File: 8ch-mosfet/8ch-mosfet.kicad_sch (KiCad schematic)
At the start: 7 parts, among them U1 ESP32-DEVKITC

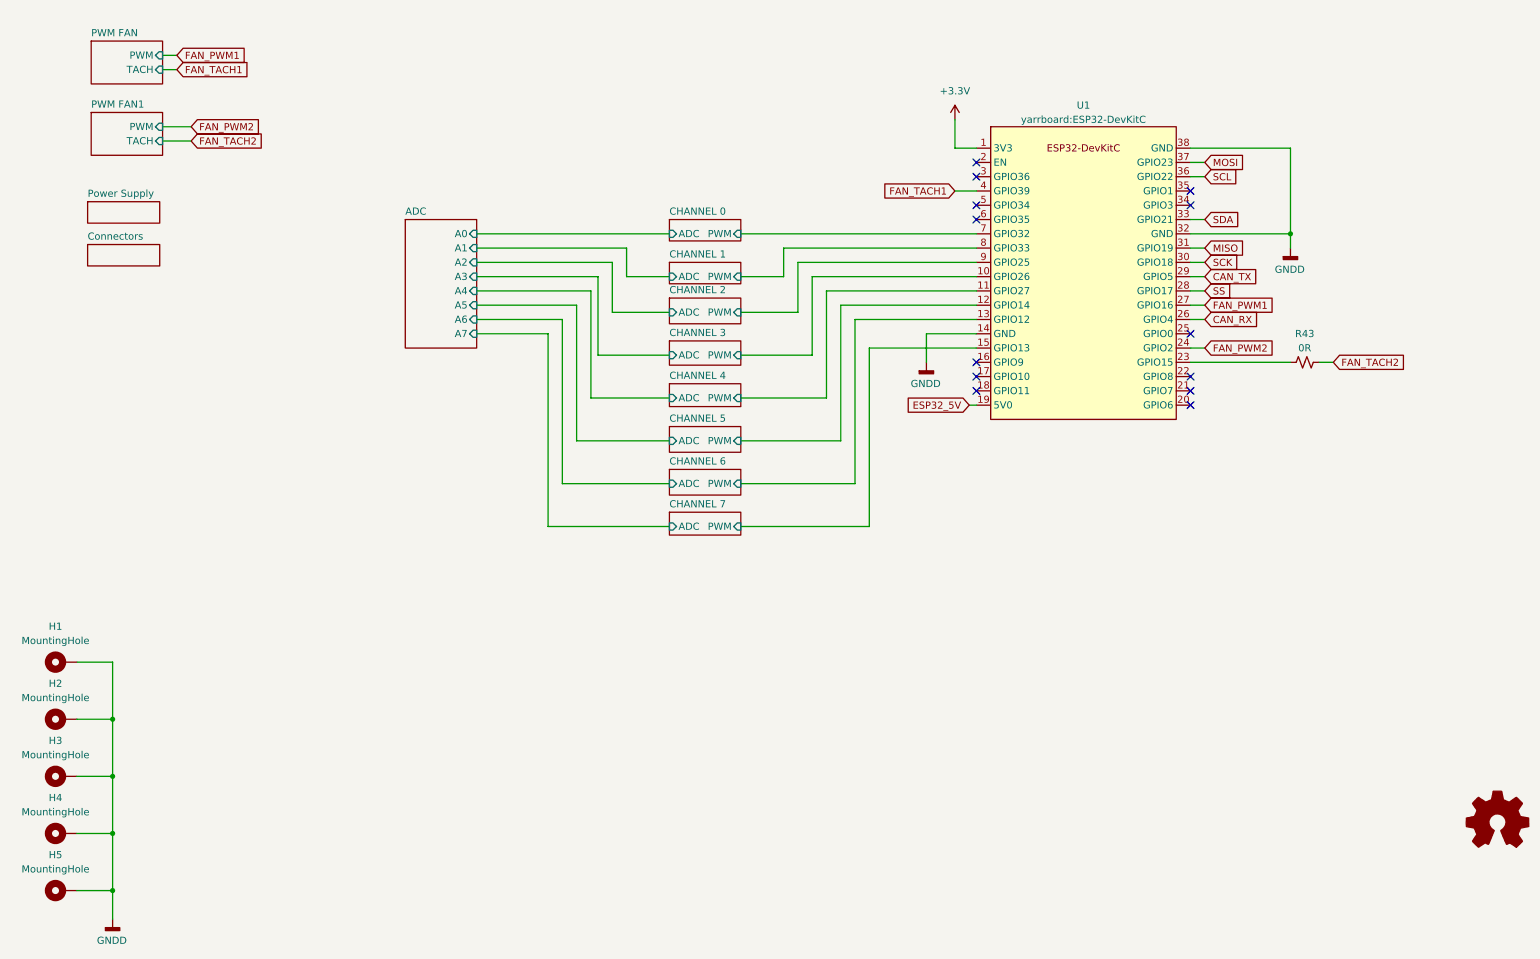
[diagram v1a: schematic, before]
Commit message: changed to new s3 module
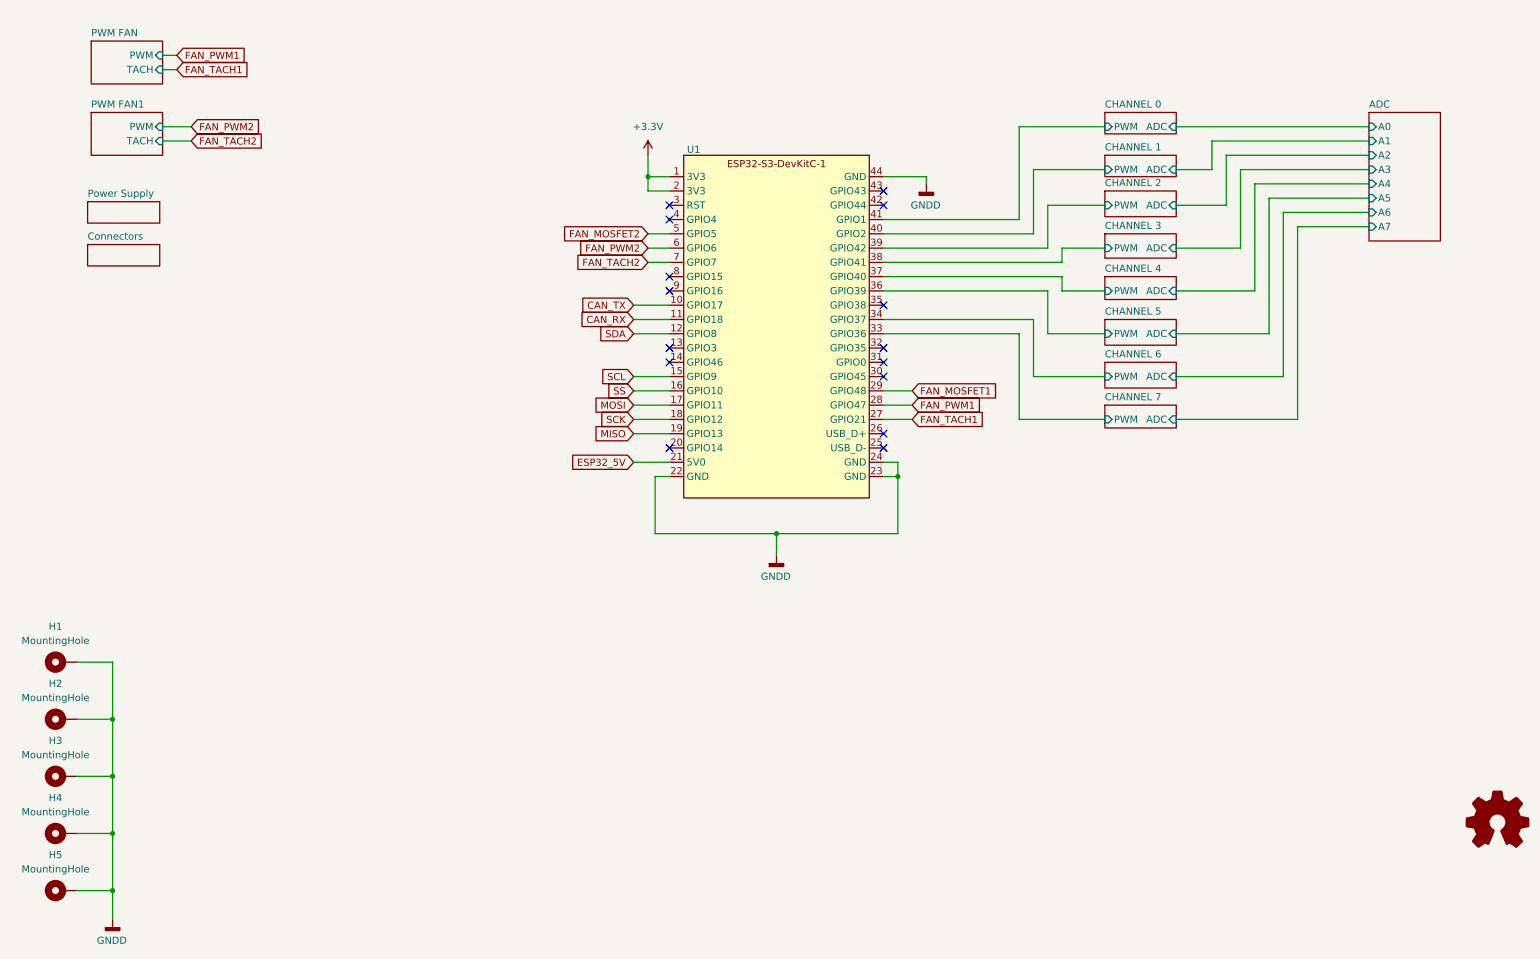
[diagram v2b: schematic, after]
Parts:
- removed R43: 0R, Resistor_SMD:R_0805_2012Metric_Pad1.20x1.40mm_HandSolder, symbol Device:R_Small_US
- removed U1: ESP32-DEVKITC, yarrboard:ESP32-DevKitC, symbol gnarboard:ESP32_DevKit_C
- added U1: ~, yarrboard:Waveshare-ESP32-S3-dev-kit, symbol yarrboard:ESP32-S3-DevKitC-1
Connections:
- net +3.3V: now also U1.1 (3V3), U1.2 (3V3)
- net CAN_RX: now also U1.11 (GPIO18)
- net CAN_TX: now also U1.10 (GPIO17)
- net CHANNEL 0/PWM: now also U1.41 (GPIO1)
- net CHANNEL 1/PWM: now also U1.40 (GPIO2)
- net CHANNEL 2/PWM: now also U1.39 (GPIO42)
- net CHANNEL 3/PWM: now also U1.38 (GPIO41)
- net CHANNEL 4/PWM: now also U1.37 (GPIO40)
- net CHANNEL 5/PWM: now also U1.36 (GPIO39)
- net CHANNEL 6/PWM: now also U1.34 (GPIO37)
- net CHANNEL 7/PWM: now also U1.33 (GPIO36)
- net ESP32_5V: now also U1.21 (5V0)
- net FAN_PWM1: now also U1.28 (GPIO47)
- net FAN_PWM2: now also U1.6 (GPIO6)
- net FAN_TACH1: now also U1.27 (GPIO21)
- net FAN_TACH2: now also U1.7 (GPIO7)
- net GNDD: now also U1.22 (GND), U1.23 (GND), U1.24 (GND), U1.44 (GND)
- net MISO: now also U1.19 (GPIO13)
- net MOSI: now also U1.17 (GPIO11)
- net SCK: now also U1.18 (GPIO12)
- net SCL: now also U1.15 (GPIO9)
- net SDA: now also U1.12 (GPIO8)
- net SS: now also U1.16 (GPIO10)
- new net FAN_MOSFET1: U1.29 (GPIO48)
- new net FAN_MOSFET2: U1.5 (GPIO5)
- no-connect marks 13 -> 15

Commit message: more progress on new 8ch board.
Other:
- sheet PWM FAN ports: added MOSFET; removed none
- sheet PWM FAN1 ports: added MOSFET; removed none
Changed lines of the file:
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@@
 	(wire
 		(pts
-			(xy 40.64 40.64) (xy 43.18 40.64)
+			(xy 40.64 38.1) (xy 45.72 38.1)
 		)
 		(stroke
@@
 	(wire
 		(pts
+			(xy 40.64 55.88) (xy 45.72 55.88)
+		)
+		(stroke
+			(width 0)
+			(type default)
+		)
+	)
+	(wire
+		(pts
 			(xy 130.81 62.23) (xy 127 62.23)
 		)
@@
 	(wire
 		(pts
+			(xy 40.64 40.64) (xy 45.72 40.64)
+		)
+		(stroke
+			(width 0)
+			(type default)
+		)
+	)
+	(wire
+		(pts
 			(xy 171.45 110.49) (xy 171.45 113.03)
 		)
@@
 	(wire
 		(pts
-			(xy 40.64 38.1) (xy 43.18 38.1)
+			(xy 40.64 35.56) (xy 45.72 35.56)
 		)
 		(stroke
@@
 		)
 	)
+	(global_label "FAN_MOSFET1"
+		(shape input)
+		(at 45.72 40.64 0)
+		(fields_autoplaced yes)
+		(effects
+			(font
+				(size 1.27 1.27)
+			)
+			(justify left)
+		)
+		(property "Intersheetrefs" "${INTERSHEET_REFS}"
+			(at 61.5866 40.64 0)
+			(effects
+				(font
+					(size 1.27 1.27)
+				)
+				(justify left)
+				(hide yes)
+			)
+		)
+	)
 	(global_label "FAN_PWM1"
 		(shape input)
@@
 	(global_label "FAN_PWM1"
 		(shape input)
-		(at 43.18 38.1 0)
+		(at 45.72 35.56 0)
 		(fields_autoplaced yes)
 		(effects
@@
 		)
 		(property "Intersheetrefs" "${INTERSHEET_REFS}"
-			(at 56.0228 38.1 0)
+			(at 58.5628 35.56 0)
 			(effects
 				(font
@@
 		)
 	)
+	(global_label "FAN_MOSFET2"
+		(shape input)
+		(at 45.72 55.88 0)
+		(fields_autoplaced yes)
+		(effects
+			(font
+				(size 1.27 1.27)
+			)
+			(justify left)
+		)
+		(property "Intersheetrefs" "${INTERSHEET_REFS}"
+			(at 61.5866 55.88 0)
+			(effects
+				(font
+					(size 1.27 1.27)
+				)
+				(justify left)
+				(hide yes)
+			)
+		)
+	)
 	(global_label "FAN_PWM2"
 		(shape input)
@@
 	(global_label "FAN_TACH1"
 		(shape input)
-		(at 43.18 40.64 0)
+		(at 45.72 38.1 0)
 		(fields_autoplaced yes)
 		(effects
@@
 		)
 		(property "Intersheetrefs" "${INTERSHEET_REFS}"
-			(at 56.5067 40.64 0)
+			(at 59.0467 38.1 0)
 			(effects
 				(font
@@
 	(sheet
 		(at 27.94 48.26)
-		(size 12.7 7.62)
+		(size 12.7 10.16)
 		(fields_autoplaced yes)
 		(stroke
@@
 		)
 		(property "Sheetfile" "pwm fan.kicad_sch"
-			(at 27.94 56.4646 0)
+			(at 27.94 59.0046 0)
 			(effects
 				(font
@@
 		(pin "TACH" input
 			(at 40.64 53.34 0)
+			(effects
+				(font
+					(size 1.27 1.27)
+				)
+				(justify right)
+			)
+		)
+		(pin "MOSFET" input
+			(at 40.64 55.88 0)
 			(effects
 				(font
@@
 	)
 	(sheet
-		(at 27.94 35.56)
-		(size 12.7 7.62)
+		(at 27.94 33.02)
+		(size 12.7 9.906)
 		(fields_autoplaced yes)
 		(stroke
@@
 		)
 		(property "Sheetname" "PWM FAN"
-			(at 27.94 34.8484 0)
+			(at 27.94 32.3084 0)
 			(effects
 				(font
@@
 		)
 		(property "Sheetfile" "pwm fan.kicad_sch"
-			(at 27.94 43.7646 0)
+			(at 27.94 43.5106 0)
 			(effects
 				(font
@@
 		)
 		(pin "PWM" input
+			(at 40.64 35.56 0)
+			(effects
+				(font
+					(size 1.27 1.27)
+				)
+				(justify right)
+			)
+		)
+		(pin "TACH" input
 			(at 40.64 38.1 0)
 			(effects
@@
 			)
 		)
-		(pin "TACH" input
+		(pin "MOSFET" input
 			(at 40.64 40.64 0)
 			(effects

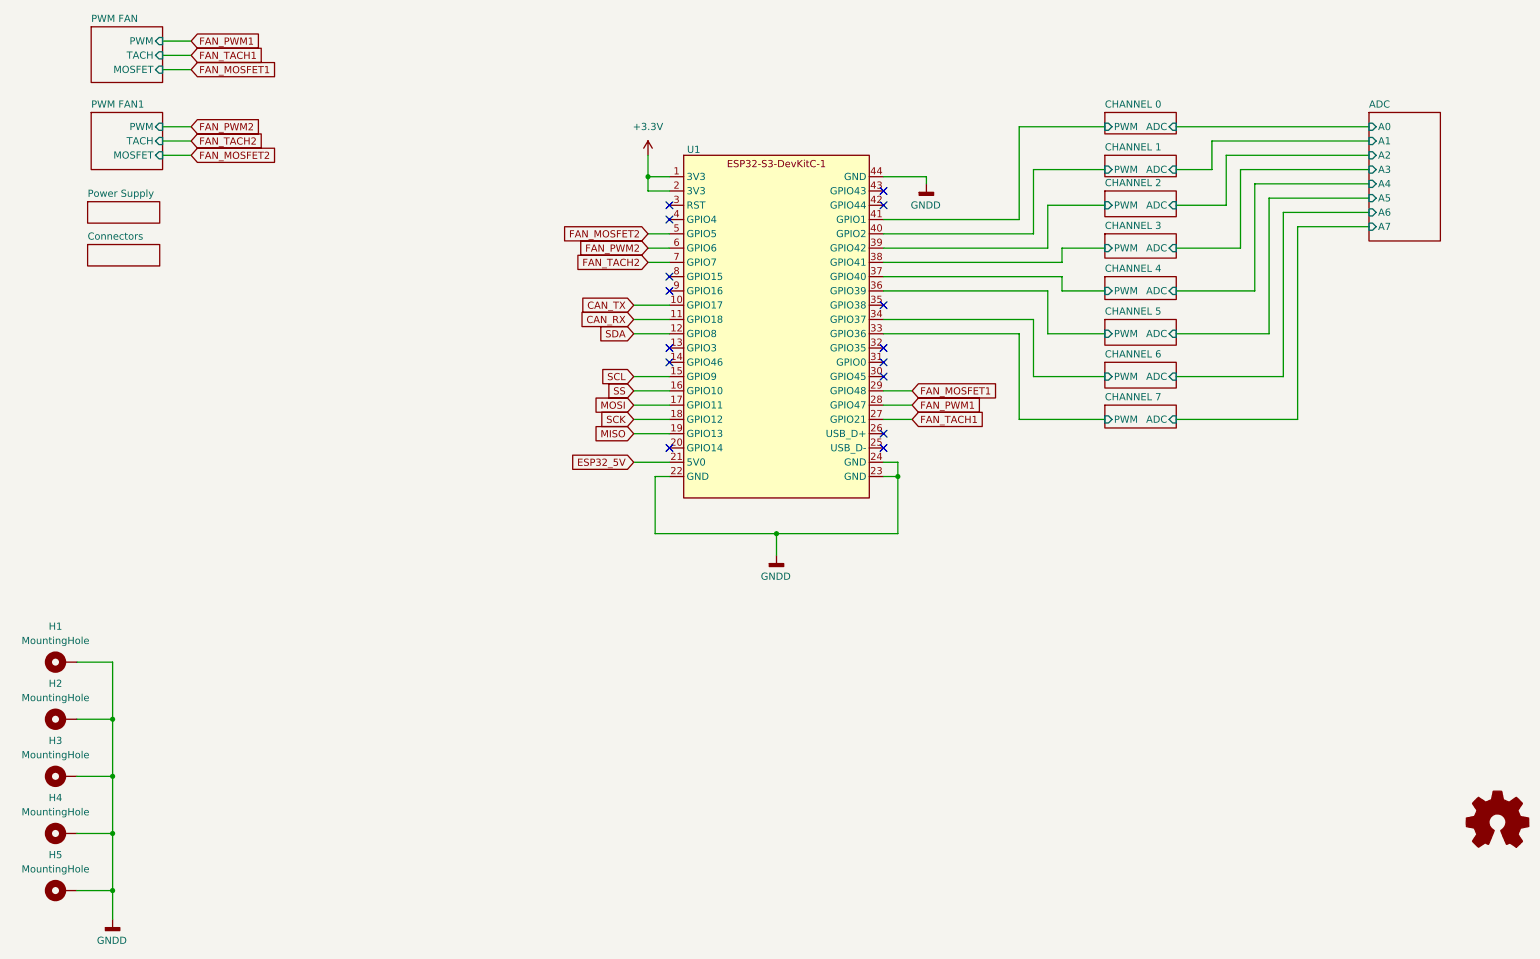
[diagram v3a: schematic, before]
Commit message: big update - 12ch, volt adc, senders, etc.
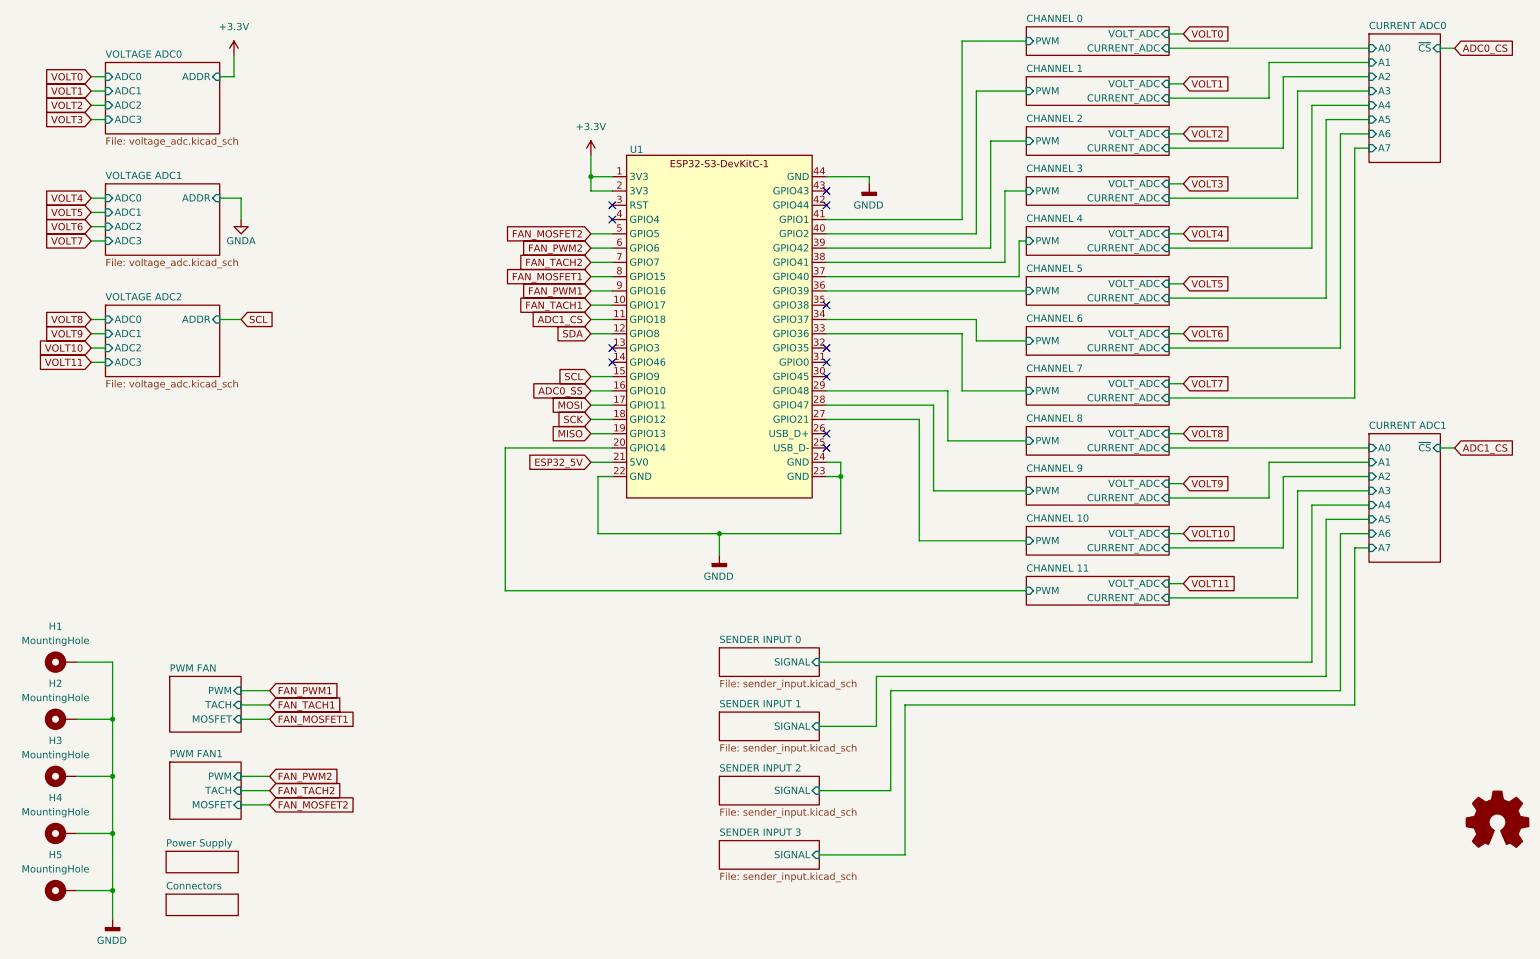
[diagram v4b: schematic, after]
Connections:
- net CAN_TX is gone; now on net FAN_TACH1: U1.10 (GPIO17)
- net FAN_MOSFET1: now also U1.8 (GPIO15); no longer U1.29 (GPIO48)
- net FAN_PWM1: now also U1.9 (GPIO16); no longer U1.28 (GPIO47)
- net FAN_TACH1: no longer U1.27 (GPIO21)
- net CHANNEL 11/PWM: now reaches U1.20 (GPIO14)
- net CAN_RX renamed ADC1_CS
- net SS renamed ADC0_SS
- new net CHANNEL 10/PWM: U1.27 (GPIO21)
- new net CHANNEL 8/PWM: U1.29 (GPIO48)
- new net CHANNEL 9/PWM: U1.28 (GPIO47)
- no-connect marks 15 -> 12
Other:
- sheet ADC renamed CURRENT ADC0
- added sheet CHANNEL 10 (mosfet.kicad_sch)
- added sheet CHANNEL 11 (mosfet.kicad_sch)
- added sheet CHANNEL 8 (mosfet.kicad_sch)
- added sheet CHANNEL 9 (mosfet.kicad_sch)
- added sheet CURRENT ADC1 (adc.kicad_sch)
- added sheet SENDER INPUT 0 (sender_input.kicad_sch)
- added sheet SENDER INPUT 1 (sender_input.kicad_sch)
- added sheet SENDER INPUT 2 (sender_input.kicad_sch)
- added sheet SENDER INPUT 3 (sender_input.kicad_sch)
- added sheet VOLTAGE ADC0 (voltage_adc.kicad_sch)
- added sheet VOLTAGE ADC1 (voltage_adc.kicad_sch)
- added sheet VOLTAGE ADC2 (voltage_adc.kicad_sch)
- sheet CHANNEL 0 ports: added CURRENT_ADC, VOLT_ADC; removed ADC
- sheet CHANNEL 1 ports: added CURRENT_ADC, VOLT_ADC; removed ADC
- sheet CHANNEL 2 ports: added CURRENT_ADC, VOLT_ADC; removed ADC
- sheet CHANNEL 3 ports: added CURRENT_ADC, VOLT_ADC; removed ADC
- sheet CHANNEL 4 ports: added CURRENT_ADC, VOLT_ADC; removed ADC
- sheet CHANNEL 5 ports: added CURRENT_ADC, VOLT_ADC; removed ADC
- sheet CHANNEL 6 ports: added CURRENT_ADC, VOLT_ADC; removed ADC
- sheet CHANNEL 7 ports: added CURRENT_ADC, VOLT_ADC; removed ADC
- sheet CURRENT ADC0 ports: added ~{CS}; removed none
- moved on the sheet: U1

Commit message: component layout looking crispy.
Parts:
- removed H2: MountingHole, MountingHole:MountingHole_3.2mm_M3_DIN965_Pad, symbol Mechanical:MountingHole_Pad
- added LOGO1: Logo_Open_Hardware_Small, Symbol:OSHW-Logo2_14.6x12mm_SilkScreen, symbol Graphic:Logo_Open_Hardware_Small
- added R1, R2: 2.2k, Resistor_SMD:R_0805_2012Metric_Pad1.20x1.40mm_HandSolder, symbol Device:R_Small_US
- renumbered H3 to H2, H4 to H3, H5 to H4
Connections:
- net CHANNEL 0/PWM is gone; now on net CHANNEL 1/PWM: U1.41 (GPIO1)
- net +3.3V: now also R1.2, R2.2
- net CHANNEL 1/PWM: no longer U1.40 (GPIO2)
- net CHANNEL 10/PWM: now also U1.28 (GPIO47); no longer U1.27 (GPIO21)
- net CHANNEL 11/PWM: now also U1.27 (GPIO21); no longer U1.20 (GPIO14)
- net CHANNEL 2/PWM: now also U1.40 (GPIO2); no longer U1.39 (GPIO42)
- net CHANNEL 3/PWM: now also U1.39 (GPIO42); no longer U1.38 (GPIO41)
- net CHANNEL 4/PWM: now also U1.38 (GPIO41); no longer U1.37 (GPIO40)
- net CHANNEL 5/PWM: now also U1.37 (GPIO40); no longer U1.36 (GPIO39)
- net CHANNEL 6/PWM: now also U1.36 (GPIO39); no longer U1.34 (GPIO37)
- net CHANNEL 7/PWM: now also U1.34 (GPIO37); no longer U1.33 (GPIO36)
- net CHANNEL 8/PWM: now also U1.33 (GPIO36); no longer U1.29 (GPIO48)
- net CHANNEL 9/PWM: now also U1.29 (GPIO48); no longer U1.28 (GPIO47)
- net SCL: now also R1.1
- net SDA: now also R2.1
- new net CHANNEL 12/PWM: U1.20 (GPIO14)
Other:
- sheet SENDER INPUT 0 renamed INPUT 1
- sheet SENDER INPUT 1 renamed INPUT 2
- sheet SENDER INPUT 2 renamed INPUT 3
- sheet SENDER INPUT 3 renamed INPUT 4
- removed sheet CHANNEL 0
- removed sheet CURRENT ADC0
- removed sheet Connectors
- removed sheet PWM FAN
- removed sheet VOLTAGE ADC0
- added sheet CHANNEL 12 (mosfet.kicad_sch)
- added sheet CURRENT ADC2 (adc.kicad_sch)
- added sheet PWM FAN2 (pwm fan.kicad_sch)
- added sheet VOLTAGE ADC3 (voltage_adc.kicad_sch)
- moved on the sheet: H1
